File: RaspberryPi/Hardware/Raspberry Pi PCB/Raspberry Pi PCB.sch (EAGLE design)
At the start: 27 parts, among them J2 1X2-3.5MM, P1 87520-0010BLF, Q11 BSS138, Q12 BSS138, U1 TPS61040QDBVRQ1, X1 0446200002

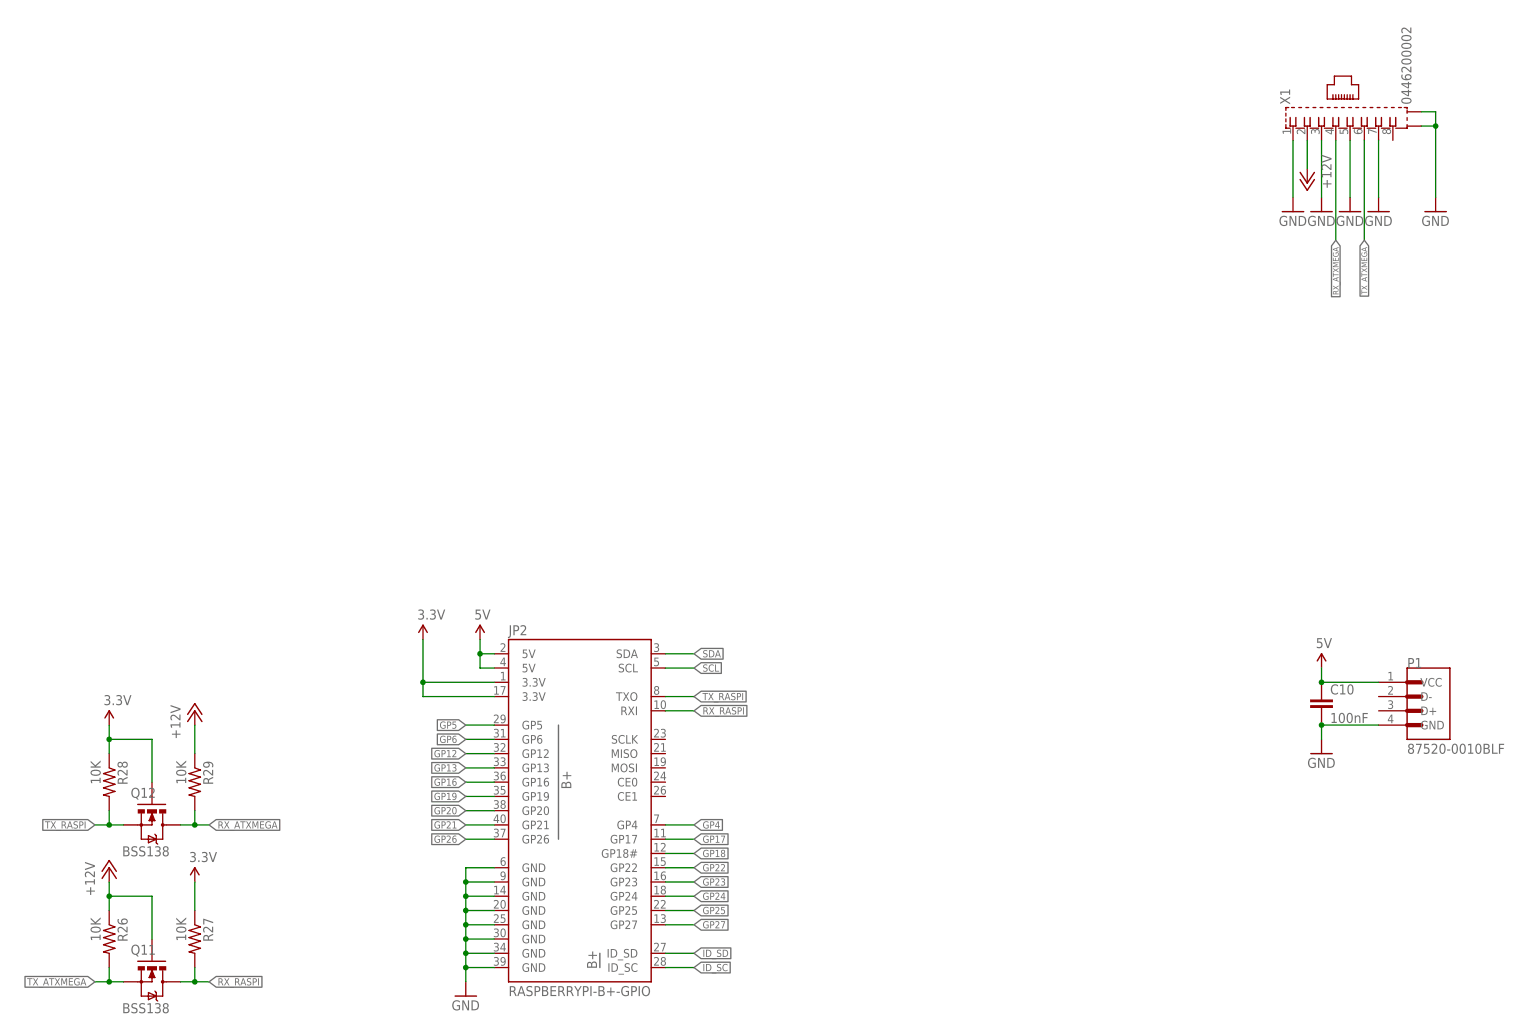
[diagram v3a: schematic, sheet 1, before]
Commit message: Many changes to the PCB design.
Most of the required components have now been included.
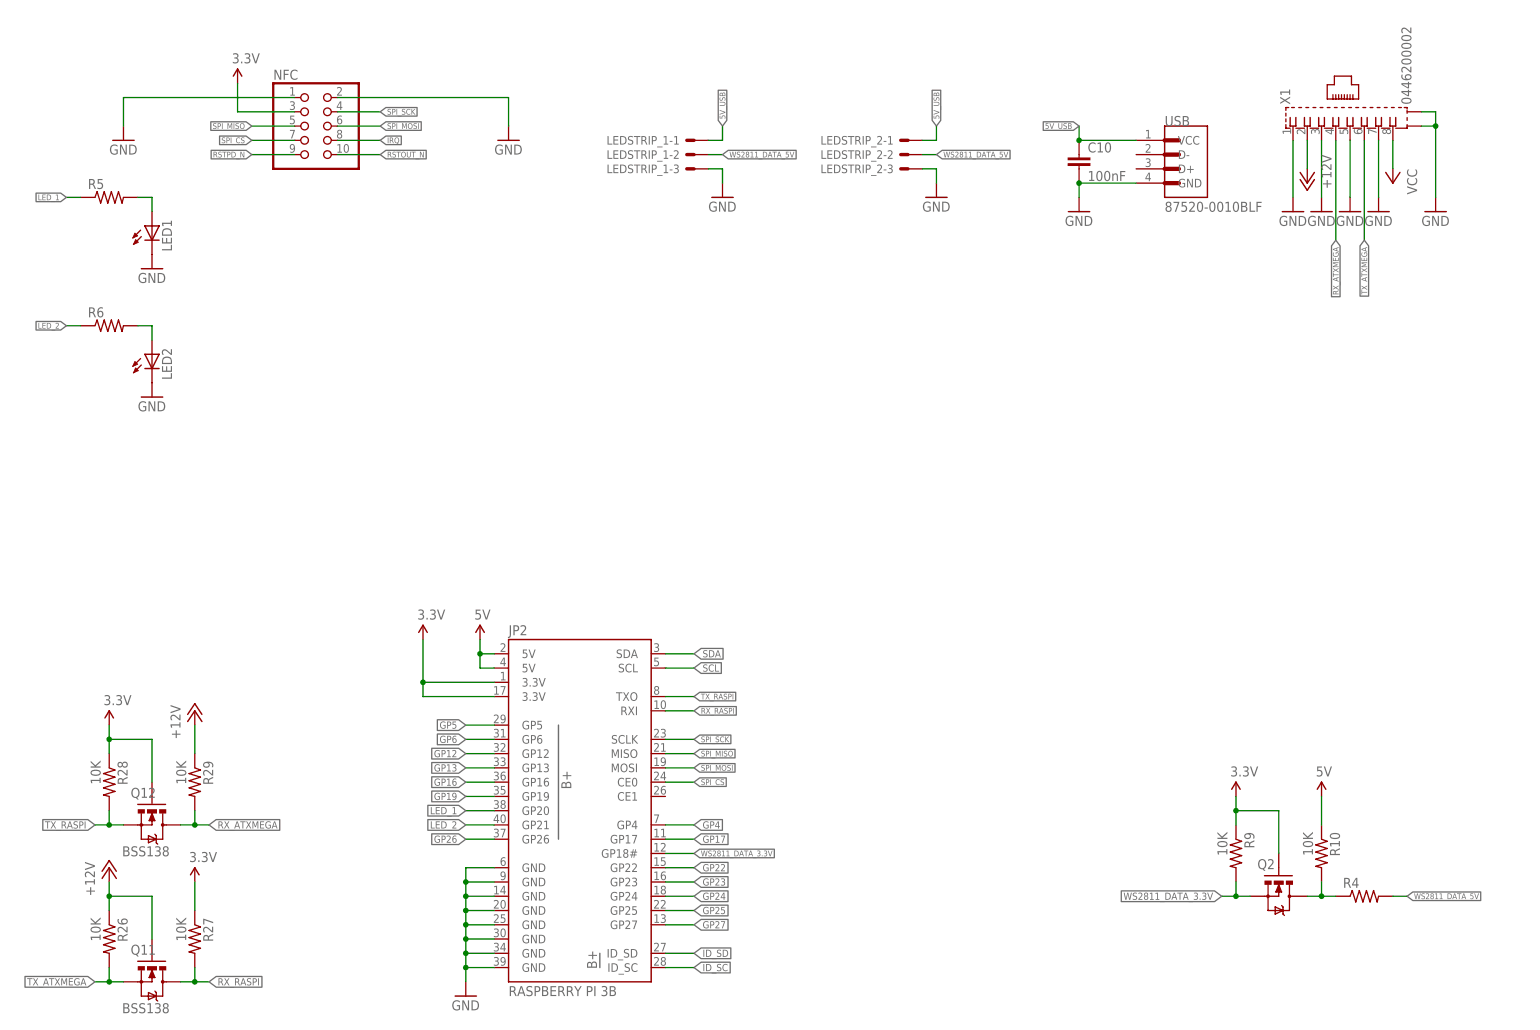
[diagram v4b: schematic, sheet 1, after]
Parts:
- removed P1: 87520-0010BLF, 87520-0010BLF:87520-0010BLF
- added C11: 100nF, SparkFun-Capacitors:1.0UF-0805-25V-(+80/-20%)
- added LED1, LED2: (no value), adafruit:LEDCHIPLED_0805
- added LEDSTRIP_1, LEDSTRIP_2: 22-05-7038-03, con-molex:22-05-7038-03
- added NFC: (no value), pinhead:PINHD-2X5
- added Q2: BSS138, SparkFun:MOSFET-NCHANNELSMD
- added R10, R9: 10K, SparkFun:RESISTOR0603-RES
- added R4, R5, R6: (no value), adafruit:R-US_R0805
- added USB: 87520-0010BLF, 87520-0010BLF:87520-0010BLF
- JP2: value RASPBERRYPI-B+-GPIO -> RASPBERRY PI 3B
- renumbered J2 to INPUT
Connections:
- removed net +5V: C1.+, C2.+, C3.1, C4.1, C5.+, C6.+, FUSE1.2, L1.1, U1.EN, U1.VIN
- removed net GP18: JP2.GP18#
- removed net GP20: JP2.GP20
- removed net GP21: JP2.GP21
- new net 5V_USB: C1.+, C10.1, C11.1, C2.+, C3.1, FUSE1.2, L1.1, LEDSTRIP_1-1.S, LEDSTRIP_2-1.S, U1.EN, U1.VIN, USB.VCC
- new net IRQ: NFC.8
- new net LED_1: JP2.GP20, R5.1
- new net LED_2: JP2.GP21, R6.1
- new net N$3: Q2.D, R10.2, R4.1
- new net N$4: LED2.A, R6.2
- new net N$5: LED1.A, R5.2
- new net RSTOUT_N: NFC.10
- new net RSTPD_N: NFC.9
- new net SPI_CS: JP2.CE0, NFC.7
- new net SPI_MISO: JP2.MISO, NFC.5
- new net SPI_MOSI: JP2.MOSI, NFC.6
- new net SPI_SCK: JP2.SCLK, NFC.4
- new net VCC: X1.8
- new net WS2811_DATA_3.3V: JP2.GP18#, Q2.S, R9.2
- new net WS2811_DATA_5V: LEDSTRIP_1-2.S, LEDSTRIP_2-2.S, R4.2
- net 3.3V: now also NFC.3, Q2.G, R9.1
- net 5V: now also C4.1, C5.+, C6.+, R10.1; no longer C10.1, P1.VCC
- net GND: now also C11.2, LED1.C, LED2.C, LEDSTRIP_1-3.S, LEDSTRIP_2-3.S, NFC.1, NFC.2, USB.GND; no longer P1.GND
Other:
- moved on the sheet: C10, C4, C5, C6

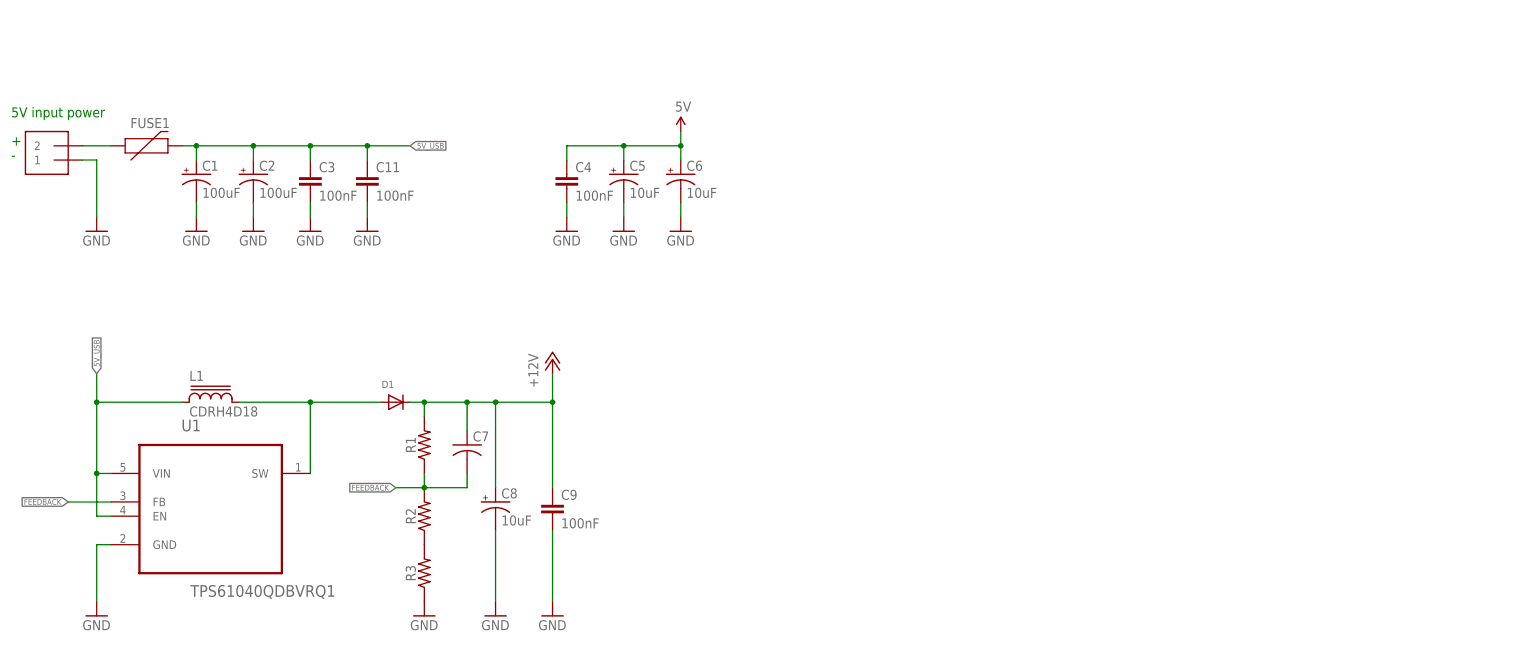
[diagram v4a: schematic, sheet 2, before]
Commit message: Removed the step up converter.
After some testing I found out that the voltage that is provided by the control PCB would be sufficient for the level conversion. This means that no boost converter is required.
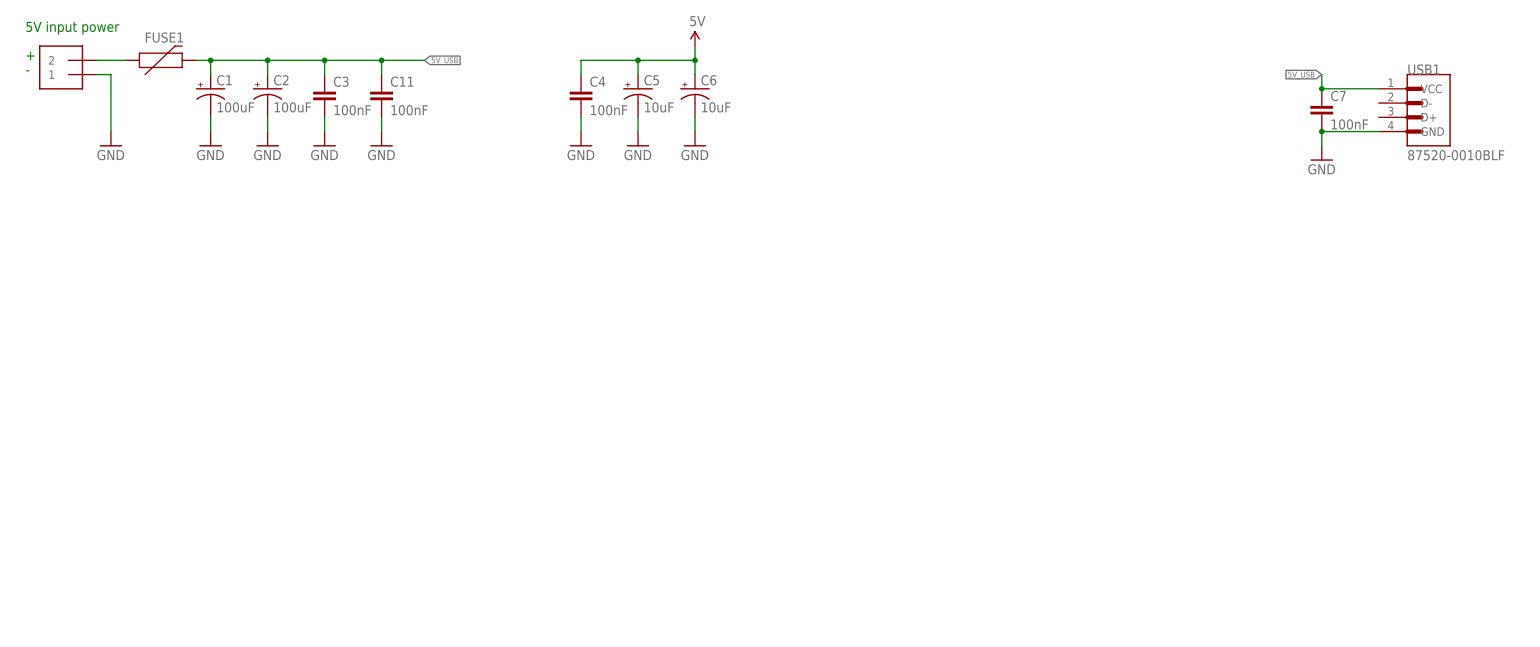
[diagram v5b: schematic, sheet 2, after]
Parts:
- removed C10, C9: 100nF, SparkFun-Capacitors:1.0UF-0805-25V-(+80/-20%)
- removed C8: 10uF, adafruit:CPOL-US153CLV-0505
- removed D1: (no value), adafruit:DIODESOD-123
- removed L1: CDRH4D18, inductor-sumida:CDRH4D18
- removed R1, R2, R3: (no value), SparkFun-Resistors:RESISTOR0805
- removed U1: TPS61040QDBVRQ1, Texas Instruments_By_element14_Batch_1:TPS61040QDBVRQ1
- removed USB: 87520-0010BLF, 87520-0010BLF:87520-0010BLF
- added USB1: 87520-0010BLF, 87520-0010BLF:87520-0010BLF
- C7: value (none) -> 100nF; device adafruit:C-USC1206 -> SparkFun-Capacitors:1.0UF-0805-25V-(+80/-20%)
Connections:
- removed net FEEDBACK: C7.2, R1.1, R2.2, U1.FB
- removed net N$1: D1.A, L1.2, U1.SW
- removed net N$2: R2.1, R3.2
- net +12V: no longer C7.1, C8.+, C9.1, D1.C, R1.2
- net 5V_USB: now also C7.1, USB1.VCC; no longer C10.1, L1.1, U1.EN, U1.VIN, USB.VCC
- net GND: now also C7.2, USB1.GND; no longer C10.2, C8.-, C9.2, R3.1, U1.GND, USB.GND
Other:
- moved on the sheet: C1, C11, C2, C3, C4, C5, C6, C7, FUSE1
